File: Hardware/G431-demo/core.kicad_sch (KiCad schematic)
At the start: 14 parts, among them U1 STM32G431CBUx, Y1 Crystal_GND24_12MHz

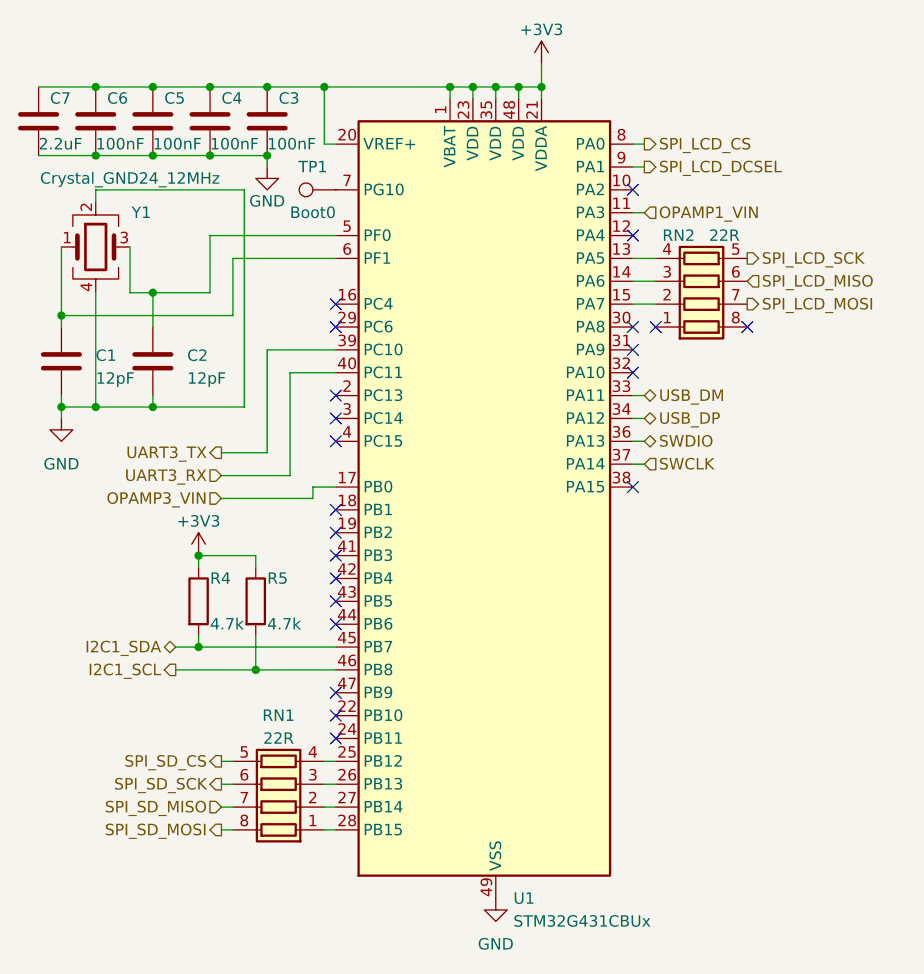
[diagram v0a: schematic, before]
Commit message: Schemetic done; PCB component layout
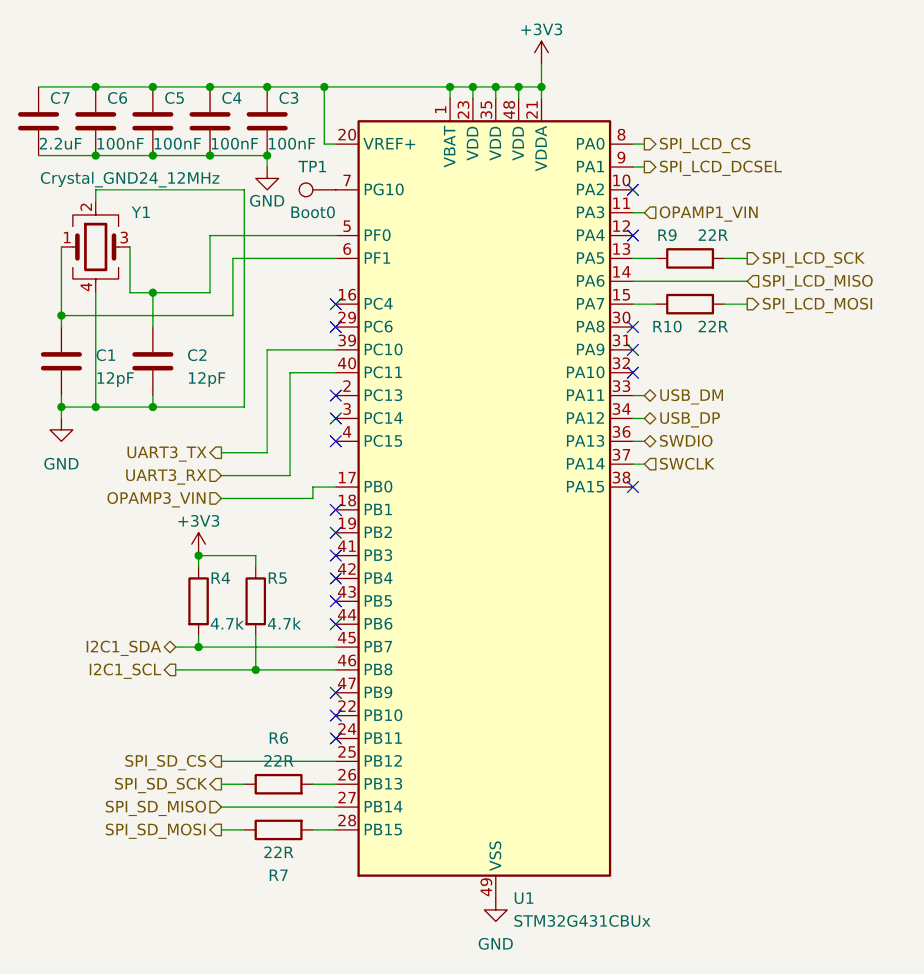
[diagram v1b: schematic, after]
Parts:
- removed RN1, RN2: 22R, Resistor_SMD:R_Array_Concave_4x0603, symbol Device:R_Pack04
- added R10, R6, R7, R9: 22R, Resistor_SMD:R_0603_1608Metric, symbol Device:R
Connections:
- net SPI_LCD_MISO: now also U1.14 (PA6)
- net SPI_LCD_MOSI: now also R10.2
- net SPI_LCD_SCK: now also R9.2
- net SPI_SD_CS: now also U1.25 (PB12)
- net SPI_SD_MISO: now also U1.27 (PB14)
- net SPI_SD_MOSI: now also R7.1
- net SPI_SD_SCK: now also R6.1
- net at U1.13 (PA5): now also R9.1
- net at U1.15 (PA7): now also R10.1
- net at U1.26 (PB13): now also R6.2
- net at U1.28 (PB15): now also R7.2
- no-connect marks 22 -> 20
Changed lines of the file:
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@@
   (no_connect (at 135.89 93.98))
   (no_connect (at 168.91 86.36))
-  (no_connect (at 181.61 83.82))
   (no_connect (at 168.91 83.82))
   (no_connect (at 135.89 104.14))
@@
   (no_connect (at 168.91 88.9))
   (no_connect (at 135.89 109.22))
-  (no_connect (at 171.45 83.82))
   (no_connect (at 135.89 124.46))
   (no_connect (at 135.89 81.28))
@@
     (stroke (width 0) (type default))
   )
-  (wire (pts (xy 123.19 132.08) (xy 124.46 132.08))
+  (wire (pts (xy 123.19 132.08) (xy 135.89 132.08))
     (stroke (width 0) (type default))
   )
@@
     (stroke (width 0) (type default))
   )
-  (wire (pts (xy 168.91 78.74) (xy 171.45 78.74))
+  (wire (pts (xy 179.07 81.28) (xy 181.61 81.28))
+    (stroke (width 0) (type default))
+  )
+  (wire (pts (xy 168.91 78.74) (xy 181.61 78.74))
     (stroke (width 0) (type default))
   )
@@
     (stroke (width 0) (type default))
   )
-  (wire (pts (xy 134.62 134.62) (xy 135.89 134.62))
+  (wire (pts (xy 133.35 134.62) (xy 135.89 134.62))
     (stroke (width 0) (type default))
   )
@@
     (stroke (width 0) (type default))
   )
+  (wire (pts (xy 179.07 76.2) (xy 181.61 76.2))
+    (stroke (width 0) (type default))
+  )
   (wire (pts (xy 124.46 82.55) (xy 105.41 82.55))
     (stroke (width 0) (type default))
@@
     (stroke (width 0) (type default))
   )
-  (wire (pts (xy 134.62 139.7) (xy 135.89 139.7))
+  (wire (pts (xy 133.35 139.7) (xy 135.89 139.7))
     (stroke (width 0) (type default))
   )
@@
     (stroke (width 0) (type default))
   )
-  (wire (pts (xy 123.19 139.7) (xy 124.46 139.7))
-    (stroke (width 0) (type default))
-  )
-  (wire (pts (xy 134.62 132.08) (xy 135.89 132.08))
+  (wire (pts (xy 123.19 139.7) (xy 125.73 139.7))
     (stroke (width 0) (type default))
   )
@@
     (stroke (width 0) (type default))
   )
-  (wire (pts (xy 134.62 137.16) (xy 135.89 137.16))
-    (stroke (width 0) (type default))
-  )
   (wire (pts (xy 120.65 119.38) (xy 135.89 119.38))
     (stroke (width 0) (type default))
@@
     (stroke (width 0) (type default))
   )
-  (wire (pts (xy 123.19 134.62) (xy 124.46 134.62))
+  (wire (pts (xy 123.19 134.62) (xy 125.73 134.62))
     (stroke (width 0) (type default))
   )
@@
     (stroke (width 0) (type default))
   )
-  (wire (pts (xy 123.19 137.16) (xy 124.46 137.16))
+  (wire (pts (xy 123.19 137.16) (xy 135.89 137.16))
     (stroke (width 0) (type default))
   )
@@
   (hierarchical_label "OPAMP1_VIN" (shape input) (at 170.18 71.12 0) (fields_autoplaced)
     (effects (font (size 1.27 1.27)) (justify left))
+  )
+  (symbol (lib_id "Device:R") (at 129.54 139.7 90) (mirror x) (unit 1)
+    (in_bom yes) (on_board yes) (dnp no)
+    (property "Reference" "R7" (at 129.54 144.78 90)
+      (effects (font (size 1.27 1.27)))
+    )
+    (property "Value" "22R" (at 129.54 142.24 90)
+      (effects (font (size 1.27 1.27)))
+    )
+    (property "Footprint" "Resistor_SMD:R_0603_1608Metric" (at 129.54 137.922 90)
+      (effects (font (size 1.27 1.27)) hide)
+    )
+    (property "Datasheet" "~" (at 129.54 139.7 0)
+      (effects (font (size 1.27 1.27)) hide)
+    )
+    (pin "1")
+    (pin "2")
+    (instances
+      (project "IR-HeatCam-G431-Demo"
+        (path "/d58afd0c-3c4a-4c6a-9275-804583496ec9/8961f4a1-cbda-4fc2-a12a-b356500549bb"
+          (reference "R7") (unit 1)
+        )
+      )
+    )
   )
   (symbol (lib_id "MCU_ST_STM32G4:STM32G431CBUx") (at 151.13 104.14 0) (unit 1)
@@
     )
   )
-  (symbol (lib_id "Device:R_Pack04") (at 129.54 134.62 90) (unit 1)
-    (in_bom yes) (on_board yes) (dnp no) (fields_autoplaced)
-    (property "Reference" "RN1" (at 129.54 127 90)
-      (effects (font (size 1.27 1.27)))
-    )
-    (property "Value" "22R" (at 129.54 129.54 90)
-      (effects (font (size 1.27 1.27)))
-    )
-    (property "Footprint" "Resistor_SMD:R_Array_Concave_4x0603" (at 129.54 127.635 90)
-      (effects (font (size 1.27 1.27)) hide)
-    )
-    (property "Datasheet" "~" (at 129.54 134.62 0)
-      (effects (font (size 1.27 1.27)) hide)
-    )
-    (pin "1")
-    (pin "2")
-    (pin "3")
-    (pin "4")
-    (pin "5")
-    (pin "6")
-    (pin "7")
-    (pin "8")
-    (instances
-      (project "IR-HeatCam-G431-Demo"
-        (path "/d58afd0c-3c4a-4c6a-9275-804583496ec9/8961f4a1-cbda-4fc2-a12a-b356500549bb"
-          (reference "RN1") (unit 1)
-        )
-      )
-    )
-  )
   (symbol (lib_id "power:+3V3") (at 120.65 109.22 0) (unit 1)
     (in_bom yes) (on_board yes) (dnp no) (fields_autoplaced)
@@
     )
   )
+  (symbol (lib_id "Device:R") (at 129.54 134.62 90) (unit 1)
+    (in_bom yes) (on_board yes) (dnp no) (fields_autoplaced)
+    (property "Reference" "R6" (at 129.54 129.54 90)
+      (effects (font (size 1.27 1.27)))
+    )
+    (property "Value" "22R" (at 129.54 132.08 90)
+      (effects (font (size 1.27 1.27)))
+    )
+    (property "Footprint" "Resistor_SMD:R_0603_1608Metric" (at 129.54 136.398 90)
+      (effects (font (size 1.27 1.27)) hide)
+    )
+    (property "Datasheet" "~" (at 129.54 134.62 0)
+      (effects (font (size 1.27 1.27)) hide)
+    )
+    (pin "1")
+    (pin "2")
+    (instances
+      (project "IR-HeatCam-G431-Demo"
+        (path "/d58afd0c-3c4a-4c6a-9275-804583496ec9/8961f4a1-cbda-4fc2-a12a-b356500549bb"
+          (reference "R6") (unit 1)
+        )
+      )
+    )
+  )
   (symbol (lib_id "Connector:TestPoint") (at 135.89 68.58 90) (unit 1)
     (in_bom yes) (on_board yes) (dnp no)
@@
         (path "/d58afd0c-3c4a-4c6a-9275-804583496ec9/8961f4a1-cbda-4fc2-a12a-b356500549bb"
           (reference "C3") (unit 1)
+        )
+      )
+    )
+  )
+  (symbol (lib_id "Device:R") (at 175.26 76.2 90) (unit 1)
+    (in_bom yes) (on_board yes) (dnp no)
+    (property "Reference" "R9" (at 172.72 73.66 90)
+      (effects (font (size 1.27 1.27)))
+    )
+    (property "Value" "22R" (at 177.8 73.66 90)
+      (effects (font (size 1.27 1.27)))
+    )
+    (property "Footprint" "Resistor_SMD:R_0603_1608Metric" (at 175.26 77.978 90)
+      (effects (font (size 1.27 1.27)) hide)
+    )
+    (property "Datasheet" "~" (at 175.26 76.2 0)
+      (effects (font (size 1.27 1.27)) hide)
+    )
+    (pin "1")
+    (pin "2")
+    (instances
+      (project "IR-HeatCam-G431-Demo"
+        (path "/d58afd0c-3c4a-4c6a-9275-804583496ec9/8961f4a1-cbda-4fc2-a12a-b356500549bb"
+          (reference "R9") (unit 1)
+        )
+      )
+    )
+  )
+  (symbol (lib_id "Device:R") (at 175.26 81.28 90) (mirror x) (unit 1)
+    (in_bom yes) (on_board yes) (dnp no)
+    (property "Reference" "R10" (at 172.72 83.82 90)
+      (effects (font (size 1.27 1.27)))
+    )
+    (property "Value" "22R" (at 177.8 83.82 90)
+      (effects (font (size 1.27 1.27)))
+    )
+    (property "Footprint" "Resistor_SMD:R_0603_1608Metric" (at 175.26 79.502 90)
+      (effects (font (size 1.27 1.27)) hide)
+    )
+    (property "Datasheet" "~" (at 175.26 81.28 0)
+      (effects (font (size 1.27 1.27)) hide)
+    )
+    (pin "1")
+    (pin "2")
+    (instances
+      (project "IR-HeatCam-G431-Demo"
+        (path "/d58afd0c-3c4a-4c6a-9275-804583496ec9/8961f4a1-cbda-4fc2-a12a-b356500549bb"
+          (reference "R10") (unit 1)
         )
       )
@@
         )
       )
-    )
-  )
-  (symbol (lib_id "Device:R_Pack04") (at 176.53 78.74 270) (mirror x) (unit 1)
-    (in_bom yes) (on_board yes) (dnp no)
-    (property "Reference" "RN2" (at 173.99 73.66 90)
-      (effects (font (size 1.27 1.27)))
-    )
-    (property "Value" "22R" (at 179.07 73.66 90)
-      (effects (font (size 1.27 1.27)))
-    )
-    (property "Footprint" "Resistor_SMD:R_Array_Concave_4x0603" (at 176.53 71.755 90)
-      (effects (font (size 1.27 1.27)) hide)
-    )
-    (property "Datasheet" "~" (at 176.53 78.74 0)
-      (effects (font (size 1.27 1.27)) hide)
-    )
-    (pin "1")
-    (pin "2")
-    (pin "3")
-    (pin "4")
-    (pin "5")
-    (pin "6")
-    (pin "7")
-    (pin "8")
-    (instances
-      (project "IR-HeatCam-G431-Demo"
-        (path "/d58afd0c-3c4a-4c6a-9275-804583496ec9/8961f4a1-cbda-4fc2-a12a-b356500549bb"
-          (reference "RN2") (unit 1)
-        )
-      )
